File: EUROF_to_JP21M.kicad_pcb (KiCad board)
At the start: 2 copper layers, 58.4 x 24.8 mm, 2 parts, among them J1 SCART-F, J2 SCART-F

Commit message: Big Updates
finished both versions, generated gerbers, created a panel with 2 of each design.
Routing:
- net A_GND: track 31.6 -> 32.5 mm
- net GND: vias 0 -> 27
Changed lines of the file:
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@@
     (thickness 1.6)
     (drawings 9)
-    (tracks 161)
+    (tracks 188)
     (zones 0)
     (modules 2)
@@
       (drillshape 0)
       (scaleselection 1)
-      (outputdirectory "Gerbers/JP21F_to_SCARTM/"))
+      (outputdirectory "Gerbers/JP21M_to_SCARTF/"))
   )
   (net 0 "")
@@
     (at 133.8 80.35 180)
     (descr "TV SCART <B>CONNECTOR</B>")
-    (fp_text reference J1 (at 21.59 -5.08 180) (layer F.SilkS)
+    (fp_text reference J1 (at 21.59 -5.08 180) (layer F.SilkS) hide
       (effects (font (size 1 1) (thickness 0.15)))
     )
     (fp_text value SCART-F (at 13.97 -5.08 180) (layer F.Fab)
       (effects (font (size 1 1) (thickness 0.15)))
-    )
-    (fp_text user "long " (at -29.083 7.747 270) (layer Dwgs.User)
-      (effects (font (size 1.6891 1.6891) (thickness 0.1778)) (justify left bottom))
-    )
-    (fp_text user "3,0 " (at -28.067 7.112 180) (layer Dwgs.User)
-      (effects (font (size 1.6891 1.6891) (thickness 0.1778)) (justify left bottom))
-    )
-    (fp_text user SCART-F (at -9.779 5.08 180) (layer F.SilkS)
-      (effects (font (size 1.6891 1.6891) (thickness 0.1778)) (justify left bottom))
-    )
-    (fp_text user long (at 31.877 7.62 270) (layer Dwgs.User)
-      (effects (font (size 1.6891 1.6891) (thickness 0.1778)) (justify left bottom))
-    )
-    (fp_text user 21 (at -21.336 2.286 180) (layer F.SilkS)
-      (effects (font (size 1.2065 1.2065) (thickness 0.127)) (justify left bottom))
-    )
-    (fp_text user 1 (at 19.939 2.286 180) (layer F.SilkS)
-      (effects (font (size 1.2065 1.2065) (thickness 0.127)) (justify left bottom))
-    )
-    (fp_text user 3,0 (at 24.765 7.112 180) (layer Dwgs.User)
-      (effects (font (size 1.6891 1.6891) (thickness 0.1778)) (justify left bottom))
     )
     (fp_line (start -24.892 -0.254) (end -24.892 3.302) (layer Edge.Cuts) (width 0.0024))
@@
     (pad 1 thru_hole oval (at 19.05 -5.08 270) (size 3.9624 1.9812) (drill 1.3208) (layers *.Cu *.Mask)
       (net 13 RT_OUT) (solder_mask_margin 0.1016))
+    (model "C:/Users/jacob/Documents/Github/Tinkerplunk-KiCAD-Footprints/Tinkerplunk.pretty/3D Models/scart-RA.wrl"
+      (offset (xyz 0 -2.2 0))
+      (scale (xyz 1 1 1))
+      (rotate (xyz 0 0 0))
+    )
   )
   (module Tinkerplunk:MALE_SCART (layer F.Cu)
     (at 113.15 93.85)
-    (fp_text reference J2 (at 20.7 -4.55) (layer F.SilkS)
+    (fp_text reference J2 (at 20.7 -4.55) (layer F.SilkS) hide
       (effects (font (size 0.9652 0.9652) (thickness 0.09652)) (justify left bottom))
     )
@@
     (fp_line (start 0 0) (end 0 0.0635) (layer F.SilkS) (width 0.12))
     (fp_line (start 0 0) (end 0 -2.54) (layer F.SilkS) (width 0.12))
-    (fp_text user 3,0 (at 24.765 7.112 180) (layer Dwgs.User)
-      (effects (font (size 1.6891 1.6891) (thickness 0.1778)) (justify left bottom))
-    )
-    (fp_text user 1 (at 19.939 2.286 180) (layer F.SilkS)
-      (effects (font (size 1.2065 1.2065) (thickness 0.127)) (justify left bottom))
-    )
-    (fp_text user 21 (at -21.336 2.286 180) (layer F.SilkS)
-      (effects (font (size 1.2065 1.2065) (thickness 0.127)) (justify left bottom))
-    )
-    (fp_text user long (at 31.877 7.62 270) (layer Dwgs.User)
-      (effects (font (size 1.6891 1.6891) (thickness 0.1778)) (justify left bottom))
-    )
-    (fp_text user SCART-F (at -9.779 5.08 180) (layer F.SilkS)
-      (effects (font (size 1.6891 1.6891) (thickness 0.1778)) (justify left bottom))
-    )
-    (fp_text user "3,0 " (at -28.067 7.112 180) (layer Dwgs.User)
-      (effects (font (size 1.6891 1.6891) (thickness 0.1778)) (justify left bottom))
-    )
-    (fp_text user "long " (at -29.083 7.747 270) (layer Dwgs.User)
-      (effects (font (size 1.6891 1.6891) (thickness 0.1778)) (justify left bottom))
-    )
     (pad 21 smd rect (at 39.575 -2) (size 2.5 4) (layers B.Cu B.Paste B.Mask)
       (net 12 GND))
@@
   (segment (start 152.725 85.555) (end 152.85 85.43) (width 0.25) (layer B.Cu) (net 12))
   (segment (start 152.725 91.85) (end 152.725 85.555) (width 0.25) (layer B.Cu) (net 12))
-  (segment (start 114.75 86.4206) (end 114.75 85.43) (width 0.25) (layer B.Cu) (net 13))
-  (segment (start 116.06561 87.73621) (end 114.75 86.4206) (width 0.25) (layer B.Cu) (net 13))
-  (segment (start 120.46121 87.73621) (end 116.06561 87.73621) (width 0.25) (layer B.Cu) (net 13))
-  (segment (start 122.325 89.6) (end 120.46121 87.73621) (width 0.25) (layer B.Cu) (net 13))
-  (segment (start 122.325 91.85) (end 122.325 89.6) (width 0.25) (layer B.Cu) (net 13))
+  (via (at 147.2 83.35) (size 0.6) (drill 0.4) (layers F.Cu B.Cu) (net 12))
+  (via (at 145.25 82.35) (size 0.6) (drill 0.4) (layers F.Cu B.Cu) (net 12))
+  (via (at 137.6 78.65) (size 0.6) (drill 0.4) (layers F.Cu B.Cu) (net 12))
+  (via (at 141.35 78.6) (size 0.6) (drill 0.4) (layers F.Cu B.Cu) (net 12))
+  (via (at 133.75 78.2) (size 0.6) (drill 0.4) (layers F.Cu B.Cu) (net 12))
+  (via (at 131.75 83.5) (size 0.6) (drill 0.4) (layers F.Cu B.Cu) (net 12))
+  (via (at 135.9 87.6) (size 0.6) (drill 0.4) (layers F.Cu B.Cu) (net 12))
+  (via (at 130 88.6) (size 0.6) (drill 0.4) (layers F.Cu B.Cu) (net 12))
+  (via (at 128.05 88.9) (size 0.6) (drill 0.4) (layers F.Cu B.Cu) (net 12))
+  (via (at 124.15 88.5) (size 0.6) (drill 0.4) (layers F.Cu B.Cu) (net 12))
+  (via (at 124.2 83.65) (size 0.6) (drill 0.4) (layers F.Cu B.Cu) (net 12))
+  (via (at 115.8 71.15) (size 0.6) (drill 0.4) (layers F.Cu B.Cu) (net 12))
+  (via (at 119.65 71.3) (size 0.6) (drill 0.4) (layers F.Cu B.Cu) (net 12))
+  (via (at 130.85 71.35) (size 0.6) (drill 0.4) (layers F.Cu B.Cu) (net 12))
+  (via (at 137.55 71.35) (size 0.6) (drill 0.4) (layers F.Cu B.Cu) (net 12))
+  (via (at 141.45 71.35) (size 0.6) (drill 0.4) (layers F.Cu B.Cu) (net 12))
+  (via (at 146.35 71.65) (size 0.6) (drill 0.4) (layers F.Cu B.Cu) (net 12))
+  (via (at 151.7 71.85) (size 0.6) (drill 0.4) (layers F.Cu B.Cu) (net 12))
+  (via (at 158.85 72) (size 0.6) (drill 0.4) (layers F.Cu B.Cu) (net 12))
+  (via (at 160.85 84.05) (size 0.6) (drill 0.4) (layers F.Cu B.Cu) (net 12))
+  (via (at 160.45 90.7) (size 0.6) (drill 0.4) (layers F.Cu B.Cu) (net 12))
+  (via (at 106.65 91.7) (size 0.6) (drill 0.4) (layers F.Cu B.Cu) (net 12))
+  (via (at 106.1 84.9) (size 0.6) (drill 0.4) (layers F.Cu B.Cu) (net 12))
+  (via (at 110.9 82.4) (size 0.6) (drill 0.4) (layers F.Cu B.Cu) (net 12))
+  (via (at 107.45 71.7) (size 0.6) (drill 0.4) (layers F.Cu B.Cu) (net 12))
+  (via (at 116 87.95) (size 0.6) (drill 0.4) (layers F.Cu B.Cu) (net 12))
+  (via (at 114.1 81.65) (size 0.6) (drill 0.4) (layers F.Cu B.Cu) (net 12))
+  (segment (start 115.48 85.43) (end 114.75 85.43) (width 0.25) (layer B.Cu) (net 13))
+  (segment (start 117.78621 87.73621) (end 115.48 85.43) (width 0.25) (layer B.Cu) (net 13))
+  (segment (start 120.68621 87.73621) (end 117.78621 87.73621) (width 0.25) (layer B.Cu) (net 13))
+  (segment (start 122.325 91.85) (end 122.325 89.375) (width 0.25) (layer B.Cu) (net 13))
+  (segment (start 122.325 89.375) (end 120.68621 87.73621) (width 0.25) (layer B.Cu) (net 13))
   (segment (start 125.59061 81.885543) (end 125.59061 78.814457) (width 0.25) (layer F.Cu) (net 14))
   (segment (start 123.225 89.6) (end 121.05439 87.42939) (width 0.25) (layer F.Cu) (net 14))
@@
   (segment (start 114.725 89.6) (end 112.98438 87.85938) (width 0.25) (layer B.Cu) (net 15))
   (segment (start 114.725 91.85) (end 114.725 89.6) (width 0.25) (layer B.Cu) (net 15))
-  (segment (start 120.465 81.3406) (end 120.465 80.35) (width 0.25) (layer B.Cu) (net 16))
-  (segment (start 114.672637 82.65621) (end 119.14939 82.65621) (width 0.25) (layer B.Cu) (net 16))
-  (segment (start 119.14939 82.65621) (end 120.465 81.3406) (width 0.25) (layer B.Cu) (net 16))
-  (segment (start 113.43439 83.894457) (end 114.672637 82.65621) (width 0.25) (layer B.Cu) (net 16))
-  (segment (start 113.43439 86.965543) (end 113.43439 83.894457) (width 0.25) (layer B.Cu) (net 16))
-  (segment (start 115.16121 87.73621) (end 114.205057 87.73621) (width 0.25) (layer B.Cu) (net 16))
-  (segment (start 114.205057 87.73621) (end 113.43439 86.965543) (width 0.25) (layer B.Cu) (net 16))
-  (segment (start 118.525 91.1) (end 115.16121 87.73621) (width 0.25) (layer B.Cu) (net 16))
-  (segment (start 118.525 91.85) (end 118.525 91.1) (width 0.25) (layer B.Cu) (net 16))
   (segment (start 120.465 82.5812) (end 120.465 80.35) (width 0.25) (layer F.Cu) (net 16))
   (segment (start 120.465 88.56) (end 120.465 82.5812) (width 0.25) (layer F.Cu) (net 16))
   (segment (start 119.425 89.6) (end 120.465 88.56) (width 0.25) (layer F.Cu) (net 16))
   (segment (start 119.425 91.85) (end 119.425 89.6) (width 0.25) (layer F.Cu) (net 16))
+  (segment (start 119.14939 82.65621) (end 120.465 81.3406) (width 0.25) (layer B.Cu) (net 16))
+  (segment (start 114.672637 82.65621) (end 119.14939 82.65621) (width 0.25) (layer B.Cu) (net 16))
+  (segment (start 120.465 81.3406) (end 120.465 80.35) (width 0.25) (layer B.Cu) (net 16))
+  (segment (start 118.525 89.575) (end 118.2 89.25) (width 0.25) (layer B.Cu) (net 16))
+  (segment (start 118.2 89.25) (end 115.718847 89.25) (width 0.25) (layer B.Cu) (net 16))
+  (segment (start 115.718847 89.25) (end 113.43439 86.965543) (width 0.25) (layer B.Cu) (net 16))
+  (segment (start 118.525 91.85) (end 118.525 89.575) (width 0.25) (layer B.Cu) (net 16))
+  (segment (start 113.43439 86.965543) (end 113.43439 83.894457) (width 0.25) (layer B.Cu) (net 16))
+  (segment (start 113.43439 83.894457) (end 114.672637 82.65621) (width 0.25) (layer B.Cu) (net 16))
   (segment (start 122.37 86.4206) (end 122.37 85.43) (width 0.25) (layer F.Cu) (net 17))
   (segment (start 123.68561 87.73621) (end 122.37 86.4206) (width 0.25) (layer F.Cu) (net 17))

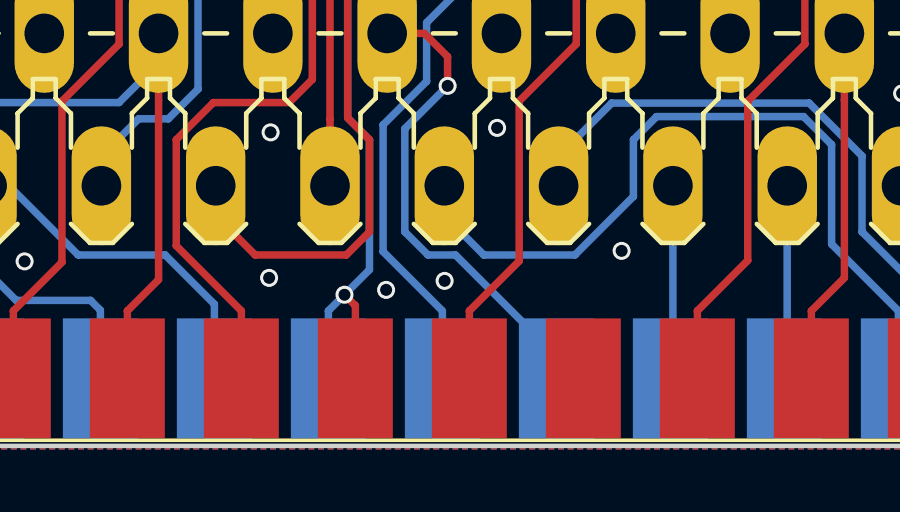
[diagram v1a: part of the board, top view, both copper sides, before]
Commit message: Fixed swapped sync pins on JP21
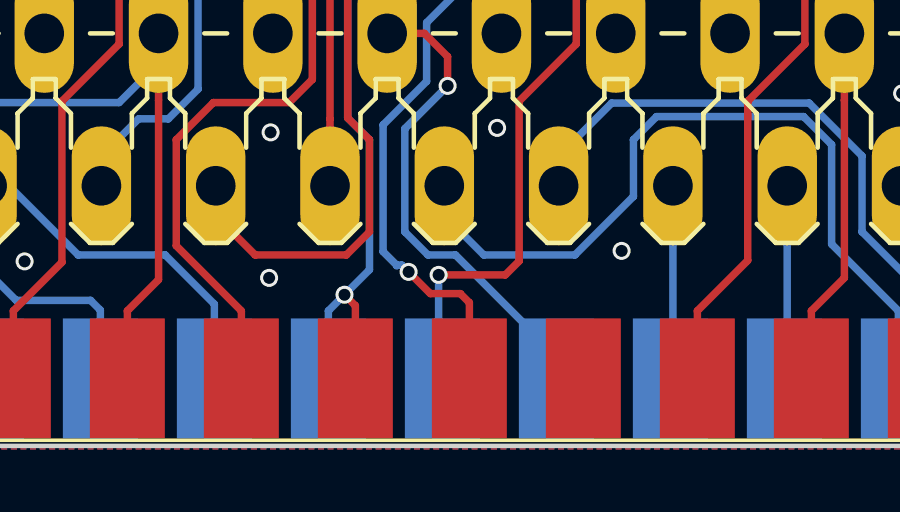
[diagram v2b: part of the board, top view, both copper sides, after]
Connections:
- J2 pad 10: S_IN -> S_OUT
- J2 pad 9: S_OUT -> S_IN
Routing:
- net S_IN: track 33.3 -> 35.2 mm, vias 0 -> 1
- net S_OUT: track 41.9 -> 43.0 mm, vias 0 -> 1
- net GND: vias 27 -> 25
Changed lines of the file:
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@@
     (thickness 1.6)
     (drawings 9)
-    (tracks 188)
+    (tracks 197)
     (zones 0)
     (modules 2)
@@
     (mod_text_size 1 1)
     (mod_text_width 0.15)
-    (pad_size 1.524 1.524)
-    (pad_drill 0.762)
+    (pad_size 2.5 4)
+    (pad_drill 0)
     (pad_to_mask_clearance 0.2)
     (aux_axis_origin 0 0)
@@
       (net 20 5V))
     (pad 9 smd rect (at 16.775 -2) (size 2.5 4) (layers B.Cu B.Paste B.Mask)
-      (net 10 S_OUT))
+      (net 11 S_IN))
     (pad 7 smd rect (at 12.975 -2) (size 2.5 4) (layers B.Cu B.Paste B.Mask)
       (net 8 S_GND))
@@
       (net 22 "Net-(J2-Pad12)"))
     (pad 10 smd rect (at 17.675 -2) (size 2.5 4) (layers F.Cu F.Paste F.Mask)
-      (net 11 S_IN))
+      (net 10 S_OUT))
     (pad 8 smd rect (at 13.875 -2) (size 2.5 4) (layers F.Cu F.Paste F.Mask)
       (net 8 S_GND))
@@
   (segment (start 138.425 89.6) (end 140.10439 87.92061) (width 0.25) (layer F.Cu) (net 9))
   (segment (start 138.425 91.85) (end 138.425 89.6) (width 0.25) (layer F.Cu) (net 9))
-  (segment (start 127.95 87.625) (end 129.925 89.6) (width 0.25) (layer B.Cu) (net 10))
-  (segment (start 127.95 83.4) (end 127.95 87.625) (width 0.25) (layer B.Cu) (net 10))
+  (segment (start 128.4 88.075) (end 128.4 88.1) (width 0.25) (layer B.Cu) (net 10))
+  (segment (start 127.95 87.625) (end 128.4 88.075) (width 0.25) (layer B.Cu) (net 10))
   (segment (start 149.04 79.403847) (end 145.736153 76.1) (width 0.25) (layer B.Cu) (net 10))
   (segment (start 149.04 85.43) (end 149.04 79.403847) (width 0.25) (layer B.Cu) (net 10))
   (segment (start 145.736153 76.1) (end 133.293847 76.1) (width 0.25) (layer B.Cu) (net 10))
   (segment (start 133.293847 76.1) (end 129.40061 79.993237) (width 0.25) (layer B.Cu) (net 10))
-  (segment (start 129.925 89.6) (end 129.925 91.85) (width 0.25) (layer B.Cu) (net 10))
+  (segment (start 127.95 83.4) (end 127.95 87.625) (width 0.25) (layer B.Cu) (net 10))
   (segment (start 129.40061 79.993237) (end 129.40061 81.94939) (width 0.25) (layer B.Cu) (net 10))
   (segment (start 129.40061 81.94939) (end 127.95 83.4) (width 0.25) (layer B.Cu) (net 10))
+  (via (at 128.8 88.3) (size 0.6) (drill 0.4) (layers F.Cu B.Cu) (net 10))
+  (segment (start 128.4 88.075) (end 128.575 88.075) (width 0.25) (layer B.Cu) (net 10))
+  (segment (start 128.575 88.075) (end 128.8 88.3) (width 0.25) (layer B.Cu) (net 10))
+  (segment (start 129.525001 89.025001) (end 130.525001 89.025001) (width 0.25) (layer F.Cu) (net 10))
+  (segment (start 128.8 88.3) (end 129.525001 89.025001) (width 0.25) (layer F.Cu) (net 10))
+  (segment (start 130.825 89.325) (end 130.825 91.85) (width 0.25) (layer F.Cu) (net 10))
+  (segment (start 130.525001 89.025001) (end 130.825 89.325) (width 0.25) (layer F.Cu) (net 10))
+  (segment (start 150.945 79.3594) (end 150.945 80.35) (width 0.25) (layer F.Cu) (net 11))
   (segment (start 149.17938 77.59378) (end 150.945 79.3594) (width 0.25) (layer F.Cu) (net 11))
   (segment (start 135.610067 77.59378) (end 149.17938 77.59378) (width 0.25) (layer F.Cu) (net 11))
+  (segment (start 132.025 88.4) (end 132.48439 87.94061) (width 0.25) (layer F.Cu) (net 11))
+  (segment (start 132.48439 87.94061) (end 132.48439 82.611763) (width 0.25) (layer F.Cu) (net 11))
+  (segment (start 132.48439 82.611763) (end 134.38939 80.706763) (width 0.25) (layer F.Cu) (net 11))
+  (segment (start 134.38939 80.706763) (end 134.38939 78.814457) (width 0.25) (layer F.Cu) (net 11))
   (segment (start 134.38939 78.814457) (end 135.610067 77.59378) (width 0.25) (layer F.Cu) (net 11))
-  (segment (start 134.38939 80.706763) (end 134.38939 78.814457) (width 0.25) (layer F.Cu) (net 11))
-  (segment (start 132.48439 82.611763) (end 134.38939 80.706763) (width 0.25) (layer F.Cu) (net 11))
-  (segment (start 132.48439 87.94061) (end 132.48439 82.611763) (width 0.25) (layer F.Cu) (net 11))
-  (segment (start 150.945 79.3594) (end 150.945 80.35) (width 0.25) (layer F.Cu) (net 11))
-  (segment (start 130.825 89.6) (end 132.48439 87.94061) (width 0.25) (layer F.Cu) (net 11))
-  (segment (start 130.825 91.85) (end 130.825 89.6) (width 0.25) (layer F.Cu) (net 11))
+  (via (at 129.8 88.4) (size 0.6) (drill 0.4) (layers F.Cu B.Cu) (net 11))
+  (segment (start 129.7 88.4) (end 129.8 88.4) (width 0.25) (layer F.Cu) (net 11))
+  (segment (start 129.8 88.4) (end 132.025 88.4) (width 0.25) (layer F.Cu) (net 11))
+  (segment (start 129.8 91.725) (end 129.925 91.85) (width 0.25) (layer B.Cu) (net 11))
+  (segment (start 129.8 88.4) (end 129.8 91.725) (width 0.25) (layer B.Cu) (net 11))
   (segment (start 152.725 85.555) (end 152.85 85.43) (width 0.25) (layer B.Cu) (net 12))
   (segment (start 152.725 91.85) (end 152.725 85.555) (width 0.25) (layer B.Cu) (net 12))
@@
   (via (at 131.75 83.5) (size 0.6) (drill 0.4) (layers F.Cu B.Cu) (net 12))
   (via (at 135.9 87.6) (size 0.6) (drill 0.4) (layers F.Cu B.Cu) (net 12))
-  (via (at 130 88.6) (size 0.6) (drill 0.4) (layers F.Cu B.Cu) (net 12))
-  (via (at 128.05 88.9) (size 0.6) (drill 0.4) (layers F.Cu B.Cu) (net 12))
   (via (at 124.15 88.5) (size 0.6) (drill 0.4) (layers F.Cu B.Cu) (net 12))
   (via (at 124.2 83.65) (size 0.6) (drill 0.4) (layers F.Cu B.Cu) (net 12))
